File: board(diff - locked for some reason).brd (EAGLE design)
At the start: 161.3 x 100 mm, 18 parts, among them IC1 ATMEGA644-20PU, Q1 2N3906, T1 2N3904, T2 2N3904, T3 2N3904, T4 2N3904

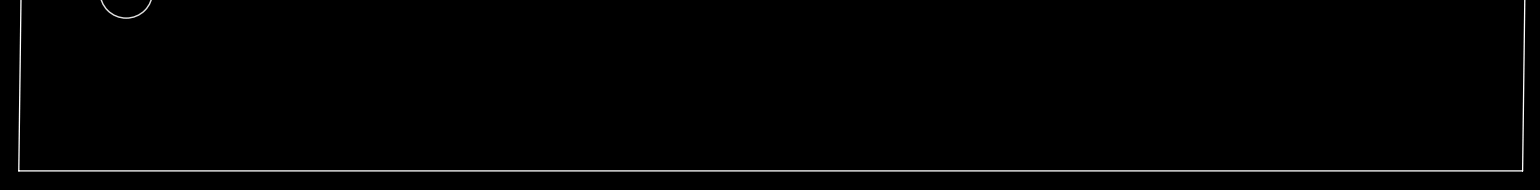
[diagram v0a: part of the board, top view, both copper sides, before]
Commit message: modified design and added ada library
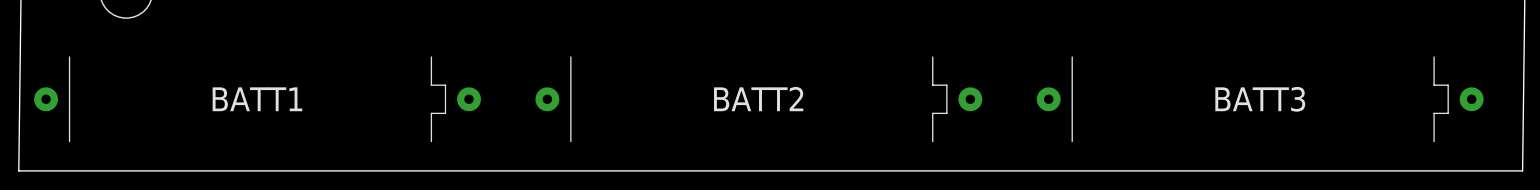
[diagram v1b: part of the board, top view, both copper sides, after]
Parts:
- added BATT1, BATT2, BATT3: AAA, adafruit:12BH412
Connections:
- removed net AVCC: IC1.30
- new net N$12: BATT1.+, BATT2.+, BATT3.+, IC1.11, IC1.31
- new net N$14: BATT1.-, BATT2.-, BATT3.-, IC1.10, IC1.30
- net GND: no longer IC1.11, IC1.31
- net VCC: no longer IC1.10
